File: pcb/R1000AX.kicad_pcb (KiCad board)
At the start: 4 copper layers, 175 x 65.5 mm, 140 parts, among them J1 PCIESOCKET-X1, J10 PCIESOCKET-X1, J11 PCIESOCKET-X1, J12 PCIESOCKET-X1, J13 PCIESOCKET-X1, J14 PCIESOCKET-X1, J15 PCIESOCKET-X1, J16 CONN127P-02X05, J17 USB_B_RECEPTACLE, J18 SOCKET254P-01X02, J19 COMPUTE_MOD_1, J2 PCIESOCKET-X1, J20 USB_A_RECEPTACLE_2, J25 SOCKET420P-02X04-CPU, J3 PCIESOCKET-X1, J31 USB_A_RECEPTACLE_2, J4 PCIESOCKET-X1, J5 PCIESOCKET-X1, J6 PCIESOCKET-X1, J7 PCIESOCKET-X1, J8 PCIESOCKET-X1, J81 SOCKET254P-01X02, J82 SOCKET254P-01X02, J83 SOCKET254P-01X02, J9 PCIESOCKET-X1, Q1 DMG2305UX-7, Q2 PSMN1R2-30YLC, Q3 Q_PNP_BEC, Q4 Q_NPN_BEC, Q5 Q_PNP_BEC, Q6 Q_PNP_BEC, U1 LPC1769FBD100,551, U2 AP3418, U20 M24C08-FDW6TP, U3 BD9E302EFJ-E2, U4 INA3221AIRGVR, U5 LM5060MM/NOPB, Y1 XTAL4_12MHz

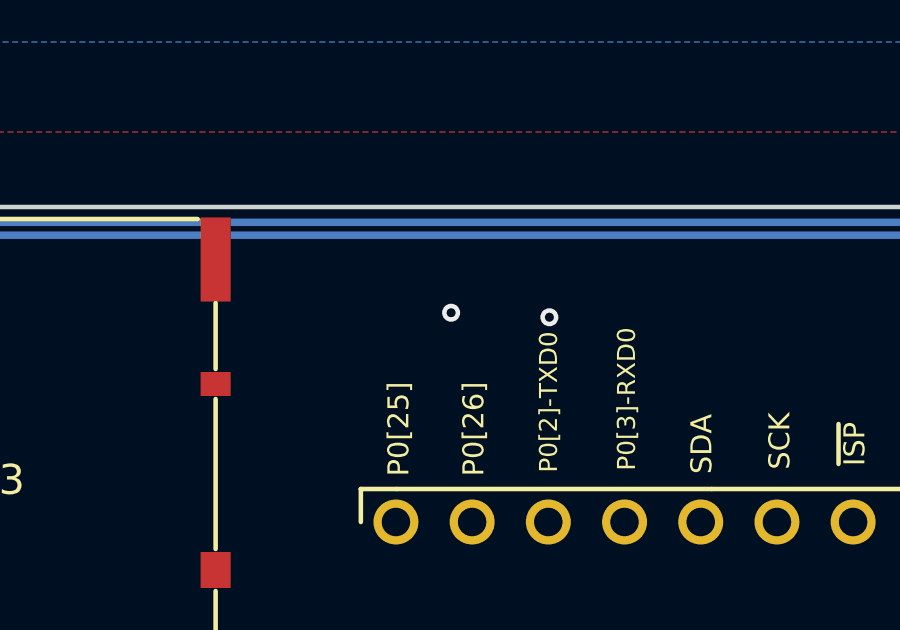
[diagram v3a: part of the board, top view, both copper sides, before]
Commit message: connected swd to compute
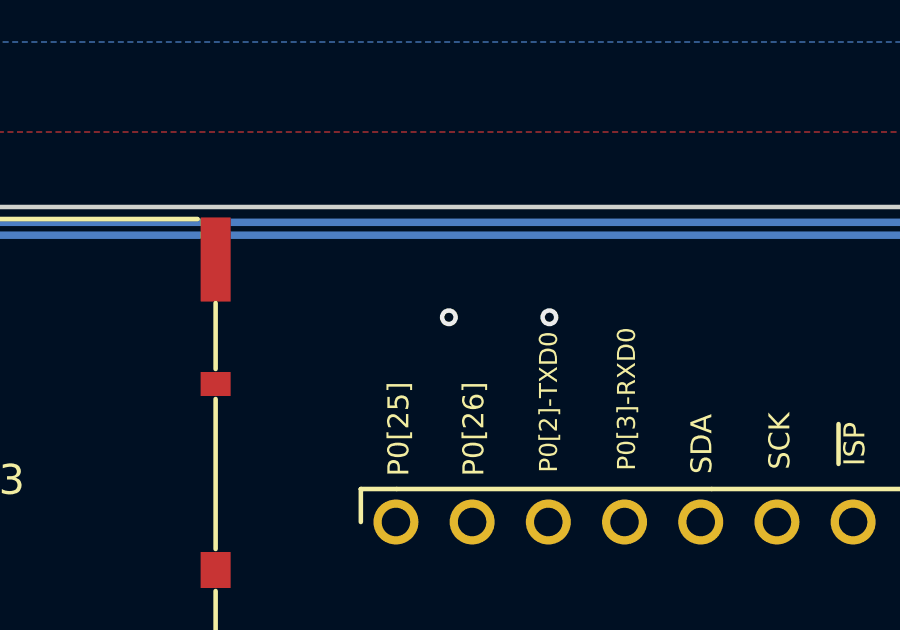
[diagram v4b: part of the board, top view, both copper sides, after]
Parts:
- R40, R41, R42, R43: value RC0603FR-070RL -> ERJ-3GEY0R00V
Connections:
- J19 pad 15: J08.PX2.A13.P0[26] -> /TCK
- J19 pad 16: J08.PX1.A12.P0[25] -> /TMS
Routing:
- net J08.PX2.A13.P0[26]: track 158.0 -> 63.3 mm, vias 2 -> 1
- net /TCK: track 15.6 -> 107.1 mm, vias 1 -> 2
- net J08.PX1.A12.P0[25]: track 154.9 -> 63.9 mm, vias 2 -> 1
- net /TMS: track 17.3 -> 103.2 mm, vias 1 -> 2

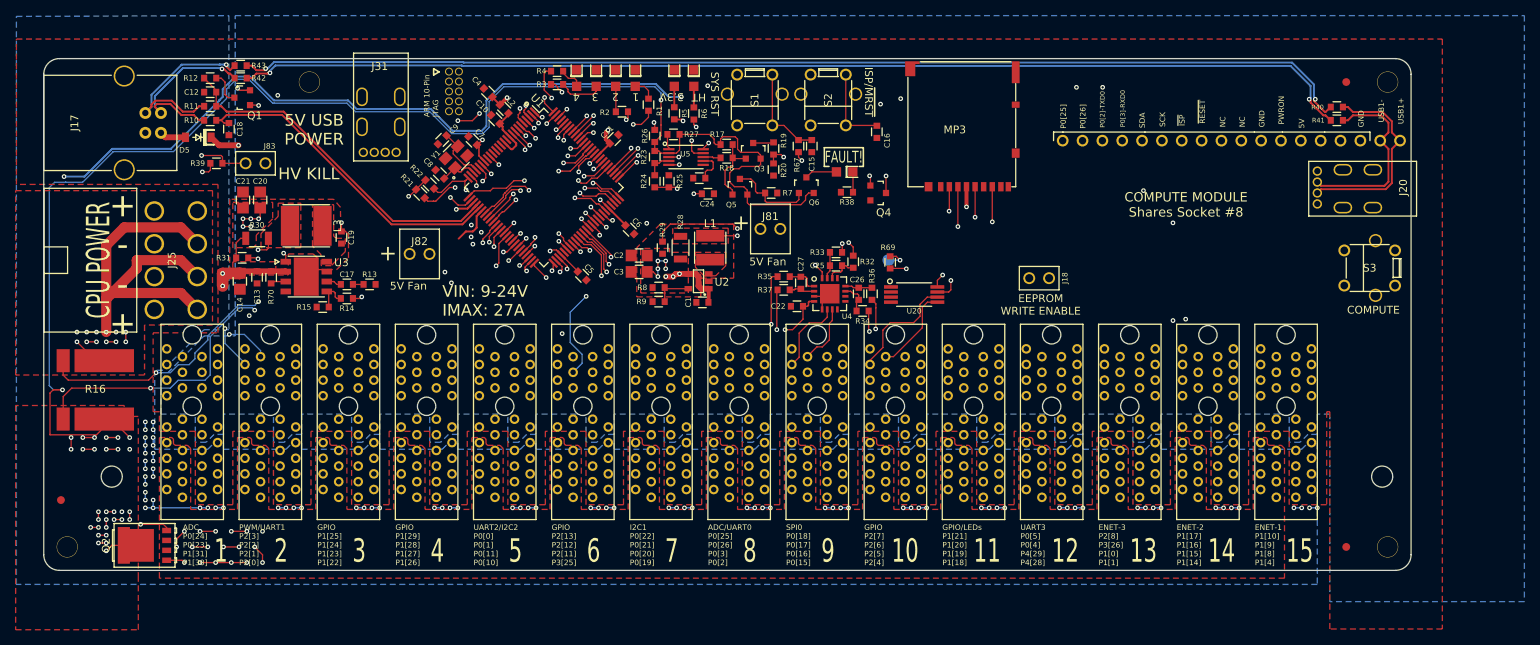
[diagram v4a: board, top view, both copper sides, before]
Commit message: added mounting holes for ubiquity robotics
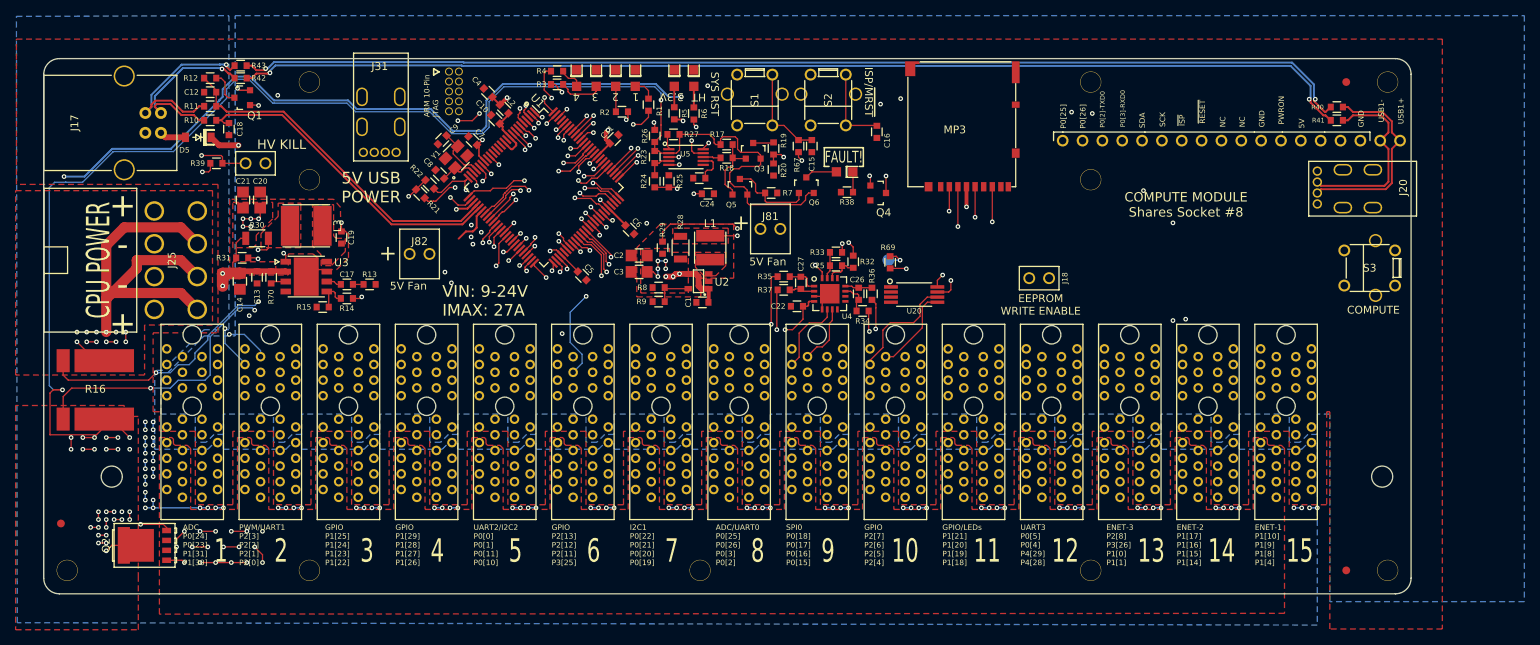
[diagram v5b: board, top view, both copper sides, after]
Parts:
- added MP1: MECH_NPTH_M3, Main:MECH_NPTH_M3, F.Cu at (85.0, 89.0)
- added MP10: MECH_NPTH_M3, Main:MECH_NPTH_M3, F.Cu at (135.0, 139.0)
- added MP11: MECH_NPTH_M3, Main:MECH_NPTH_M3, F.Cu at (85.0, 139.0)
- added MP12: MECH_NPTH_M3, Main:MECH_NPTH_M3, F.Cu at (185.0, 139.0)
- added MP5: MECH_NPTH_M3, Main:MECH_NPTH_M3, F.Cu at (185.0, 76.5)
- added MP9: MECH_NPTH_M3, Main:MECH_NPTH_M3, F.Cu at (185.0, 89.0)
- moved FID2 3.00 mm to (53.2, 133.0)
- moved FID3 3.00 mm to (217.7, 139.0)
- moved MP4 3.00 mm to (223.0, 139.0)
- moved MP7 3.00 mm to (54.0, 139.0)
- moved A1 2.68 mm to (170.0, 91.5)
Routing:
- net HT: track 325.7 -> 260.2 mm
- net /~RESET: track 126.7 -> 122.4 mm
- net /TCK: track 107.1 -> 103.0 mm
- net +5V: track 43.2 -> 46.8 mm
- net J08.PX3.A14.P0[3]: track 145.6 -> 142.9 mm
- net ~MRESET: track 329.7 -> 327.1 mm
- net /TMS: track 103.2 -> 100.7 mm
- net J08.PX4.A15.P0[2]: track 143.7 -> 141.4 mm
- net /PowerMonitor/LM5060_GATE: track 194.2 -> 192.2 mm
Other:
- board size 175 x 65.5 mm -> 175 x 68.5 mm

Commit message: replaced molex USB connector with a common connector, all USBs are low profile now
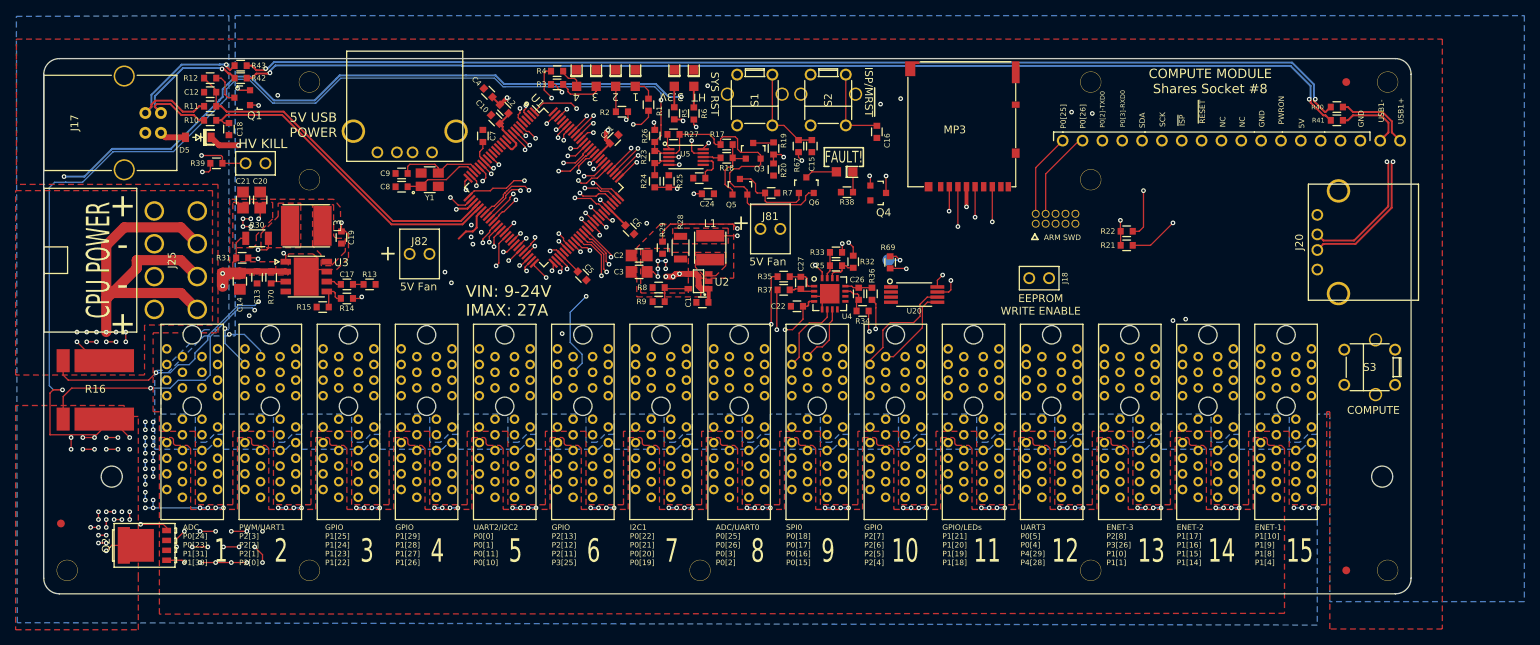
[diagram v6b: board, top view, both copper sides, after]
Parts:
- J20, J31: value USB_A_RECEPTACLE_2 -> USB_A_RECEPTACLE; footprint Main:USB_A_RECEPTACLE_2 -> Main:USB_A_RECEPTACLE
- moved R21 90.6 mm to (189.6, 97.4), turned to 0 degrees
- moved R22 89.4 mm to (189.6, 95.6), turned to 0 degrees
- moved J16 78.7 mm to (180.5, 94.0), turned to 0 degrees
- moved S3 12.7 mm to (220.7, 113.0)
- moved A1 7.00 mm to (163.0, 91.5)
- moved J20 7.00 mm to (214.0, 97.0)
- moved C9 6.75 mm to (96.8, 88.2), turned to 180 degrees
- moved C8 5.15 mm to (96.8, 89.9), turned to 180 degrees
- moved Y1 4.47 mm to (100.4, 89.0), turned to 0 degrees
- moved J31 3.20 mm to (97.2, 85.5)
- moved C7 1.43 mm to (107.2, 83.4), turned to 90 degrees
- moved A3 0.60 mm to (193.6, 91.4)
- moved A4 0.60 mm to (206.0, 90.4)
- moved A5 0.60 mm to (200.0, 102.6)
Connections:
- J16 pad 10: /~TRST -> (no net)
- J16 pad 7: /RTCK -> (no net)
- J16 pad 8: /TDI -> (no net)
- U1 pad 100: /RTCK -> (no net)
- U1 pad 2: /TDI -> (no net)
- U1 pad 4: /~TRST -> (no net)
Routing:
- net /TDO: track 15.6 -> 84.7 mm
- net /RTCK: track 20.3 -> 0.00 mm, vias 3 -> 0
- net /TDI: track 14.1 -> 0.00 mm, vias 1 -> 0
- net /PowerMonitor/LM5060_GATE: track 192.2 -> 179.0 mm
- net HV_~PGD: track 135.4 -> 122.2 mm
- net /~TRST: track 12.1 -> 0.00 mm, vias 1 -> 0
- net /PWRON: track 29.7 -> 41.1 mm
- net /P2.9: track 73.0 -> 84.0 mm
- net +5V: track 46.8 -> 53.3 mm
- net /COMPUTE_USB+: track 25.9 -> 32.3 mm, vias 0 -> 1
- net /COMPUTE_USB-: track 24.4 -> 30.3 mm, vias 0 -> 1
- net /XTAL2: track 5.01 -> 9.81 mm
- net /TMS: track 100.7 -> 96.1 mm
- net /XTAL1: track 7.03 -> 11.4 mm
- net HT: track 260.2 -> 256.0 mm
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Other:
- board text added: "ARM SWD"
- board text removed: "ARM 10-Pin JTAG"
